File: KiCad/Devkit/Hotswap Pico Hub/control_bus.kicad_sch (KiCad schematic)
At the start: 5 parts, among them J502 Devkit Hotswap Hub Port, U500 OS Buffer, U501 User Buffer

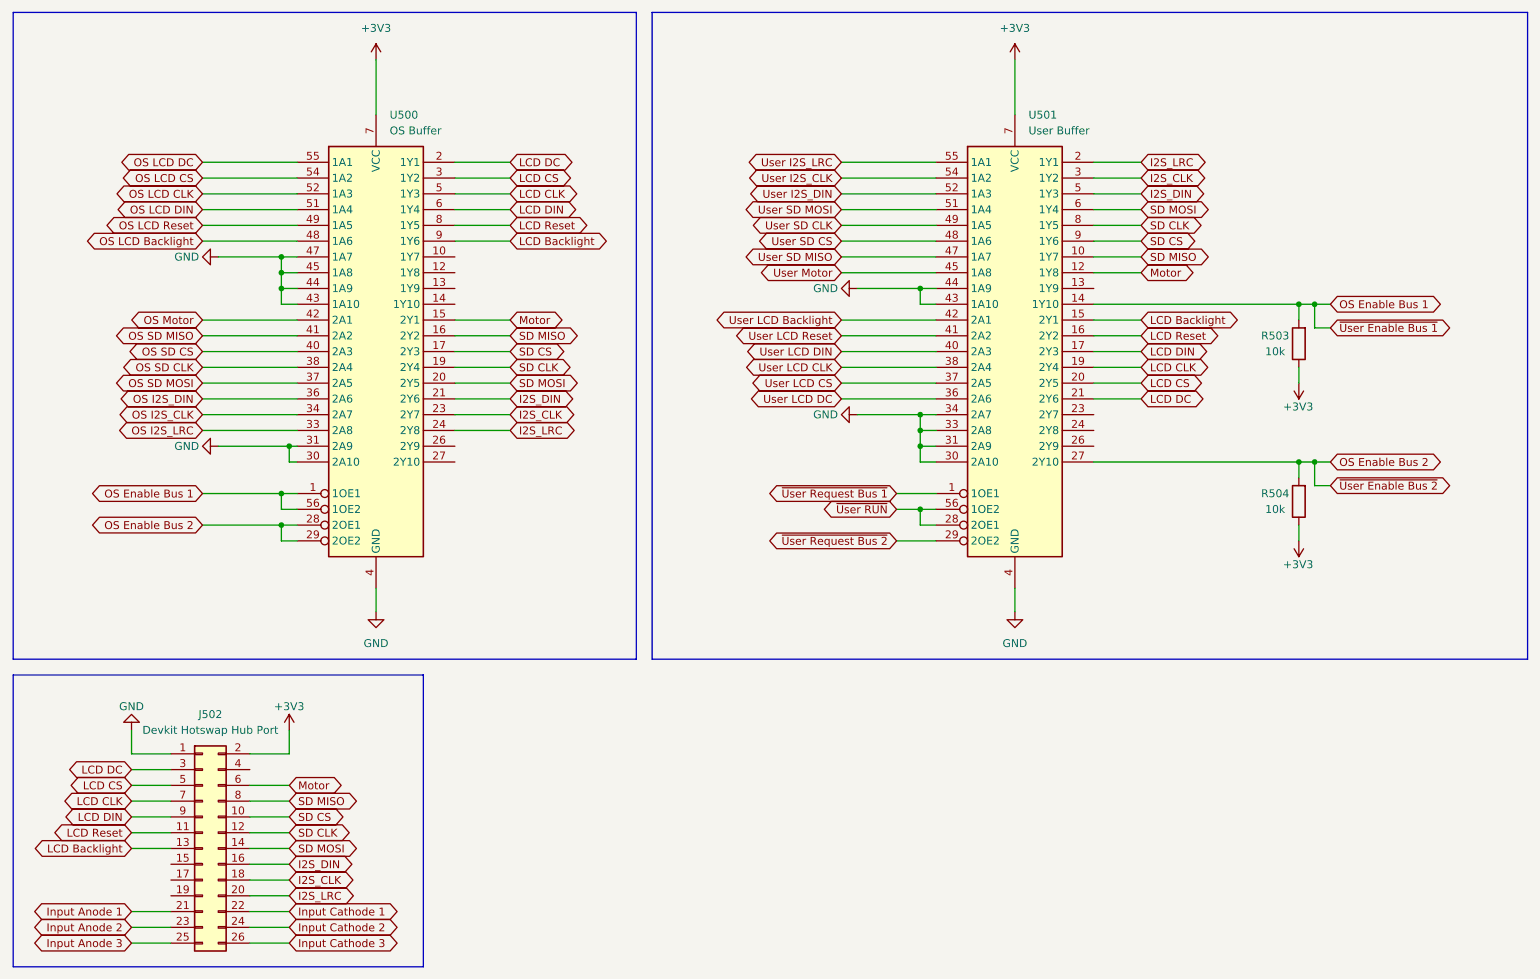
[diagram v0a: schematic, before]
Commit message: Updated KiCad to V1.1.2
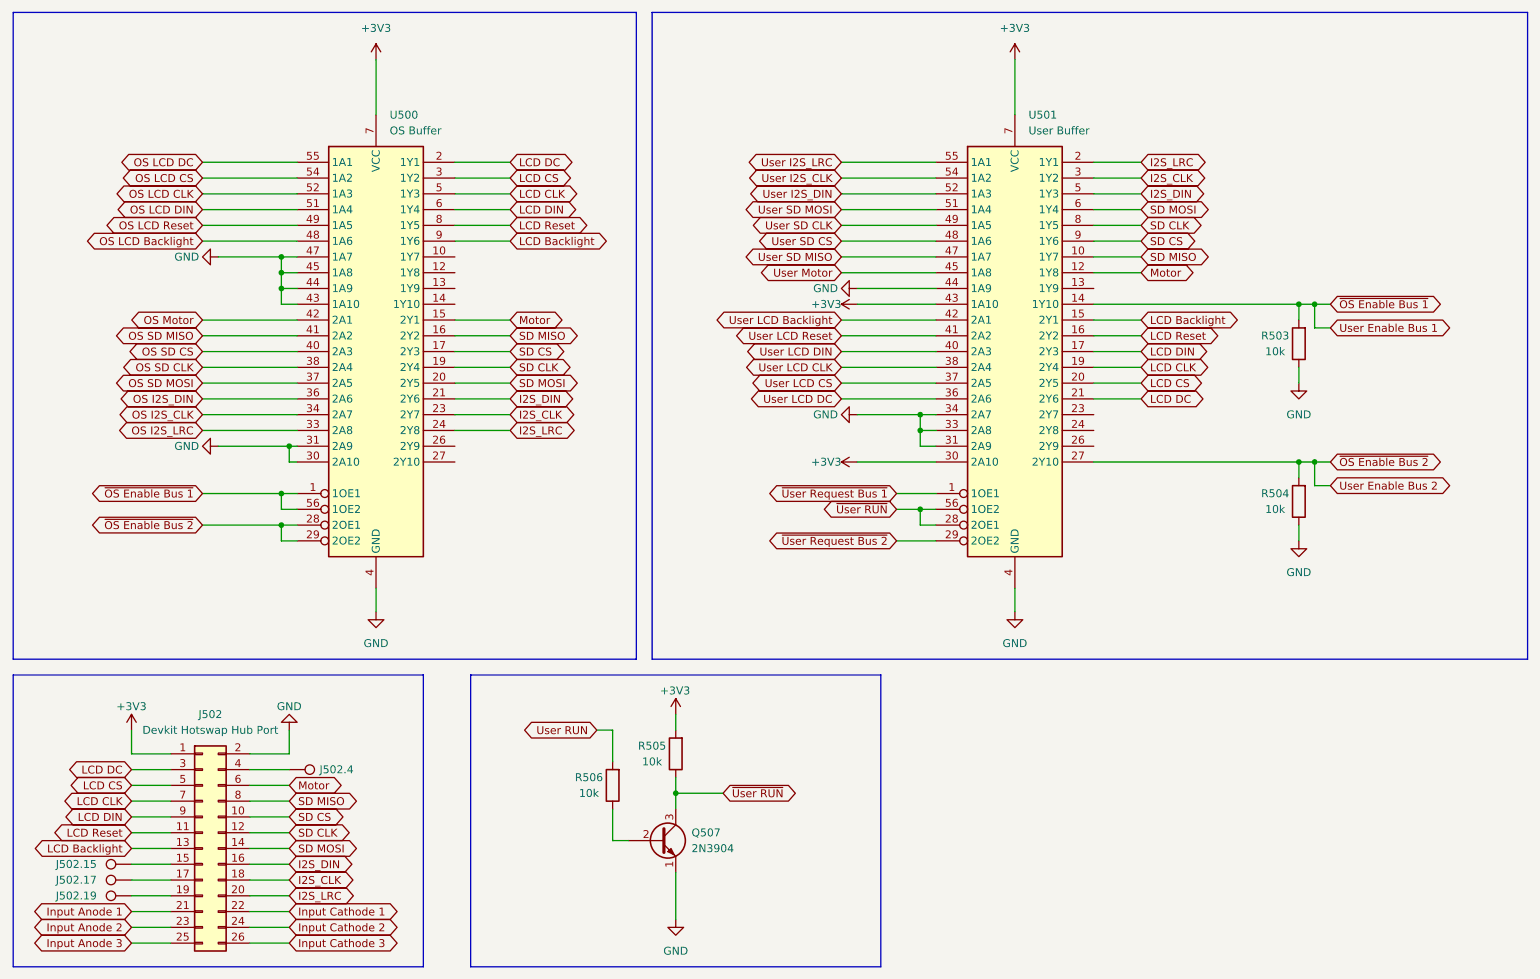
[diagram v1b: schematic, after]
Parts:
- added J502.15, J502.17, J502.19, J502.4: TestPoint, TestPoint:TestPoint_Pad_1.5x1.5mm, symbol Connector:TestPoint
- added Q507: 2N3904, Package_TO_SOT_THT:TO-92_Inline, symbol Transistor_BJT:2N3904
- added R505, R506: 10k, Resistor_SMD:R_0805_2012Metric, symbol Device:R
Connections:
- net +3V3: now also J502.1 (Pin_1), U501.30 (2A10), U501.43 (1A10), R505.2; no longer J502.2 (Pin_2), R503.1, R504.1
- net GND: now also J502.2 (Pin_2), R503.1, R504.1, Q507.1 (E); no longer J502.1 (Pin_1), U501.30 (2A10), U501.43 (1A10)
- net ~{User RUN}: now also Q507.3 (C), R505.1
- net at J502.15 (Pin_15): now also J502.15.1
- net at J502.17 (Pin_17): now also J502.17.1
- net at J502.19 (Pin_19): now also J502.19.1
- net at J502.4 (Pin_4): now also J502.4.1
- net OS Enable Bus 1 renamed User Enable Bus 1
- net OS Enable Bus 2 renamed User Enable Bus 2
- new net: Q507.2 (B), R506.1
- new net User RUN: R506.2
